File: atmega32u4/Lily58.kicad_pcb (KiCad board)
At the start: 2 copper layers, 142.5 x 106.3 mm, 96 parts, among them J2 4PIN, J4 USB_C_Receptacle_USB2.0, P4 OLED, SW1 SW_PUSH, SW10 SW_PUSH, SW11 SW_PUSH, SW12 SW_PUSH, SW13 SW_PUSH, SW14 SW_PUSH, SW15 SW_PUSH, SW16 SW_PUSH, SW17 SW_PUSH, SW18 SW_PUSH, SW19 SW_PUSH, SW2 SW_PUSH, SW20 SW_PUSH, SW21 SW_PUSH, SW22 SW_PUSH, SW23 SW_PUSH, SW24 SW_PUSH, SW25 SW_PUSH, SW26 SW_PUSH, SW27 SW_PUSH, SW28 SW_PUSH, SW29 SW_PUSH, SW3 SW_PUSH, SW4 SW_PUSH, SW5 SW_PUSH, SW6 SW_PUSH, SW7 SW_PUSH, SW8 SW_PUSH, SW9 SW_PUSH, U1 ATmega32U4-AU, U2 MCP23017_SO, U3 MCP1703A-3302_SOT23, Y1 16MHz

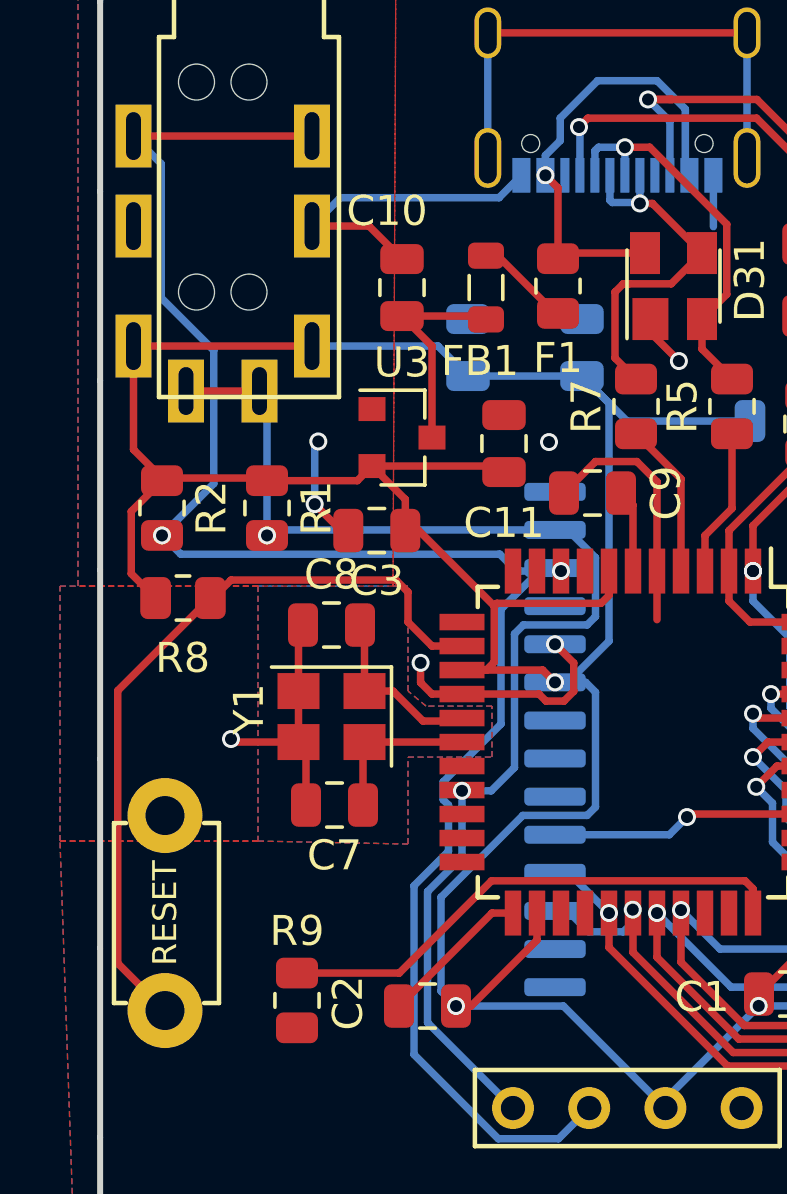
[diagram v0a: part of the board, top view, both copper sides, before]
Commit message: removing ldo on atmega32u4
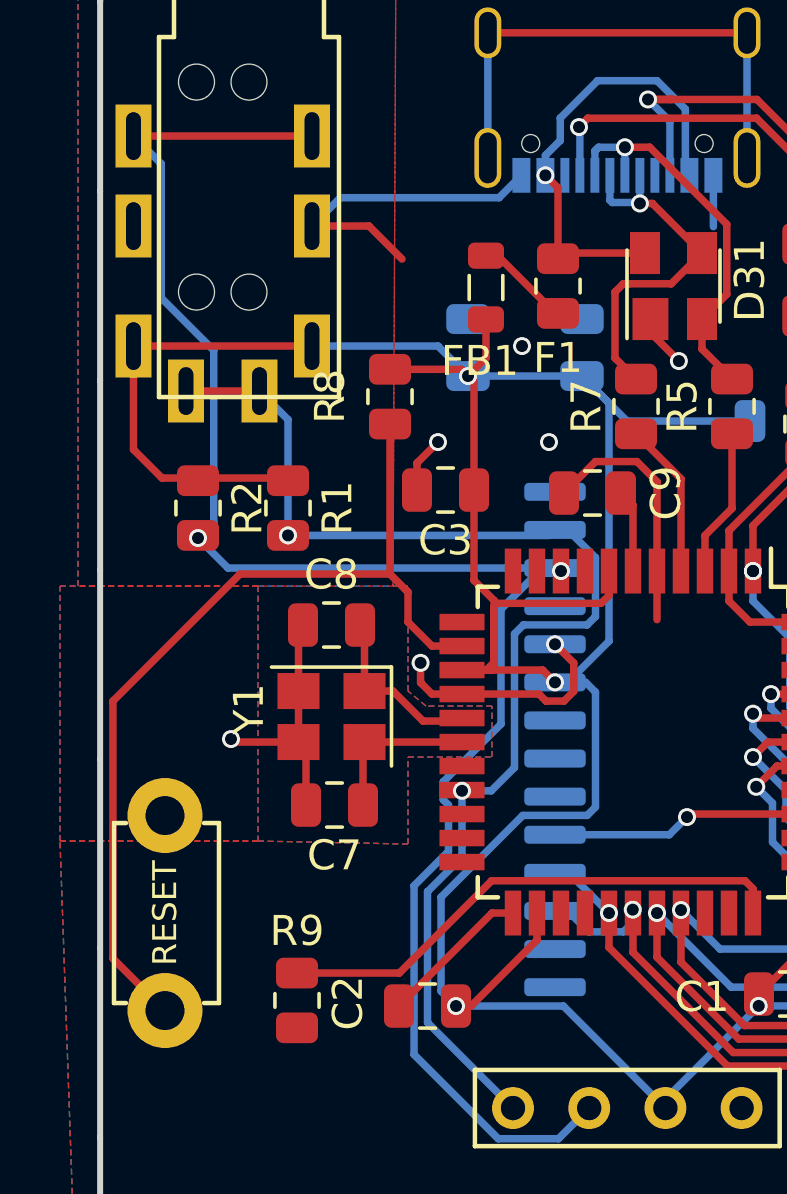
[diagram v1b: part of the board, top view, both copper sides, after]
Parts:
- removed C10, C11: 1uF, Capacitor_SMD:C_0805_2012Metric
- removed U3: MCP1703A-3302_SOT23, Package_TO_SOT_SMD:SOT-23
- moved R8 9.63 mm to (92.6, 51.3), turned to 270 degrees
- moved C3 2.66 mm to (94.5, 54.4)
- moved R2 1.20 mm to (86.2, 55.0)
- moved R1 0.70 mm to (89.2, 55.0)
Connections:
- C1 pad 1: +3V3 -> +5V
- C2 pad 1: +3V3 -> +5V
- C3 pad 1: +3V3 -> +5V
- C4 pad 1: +3V3 -> +5V
- C5 pad 1: +3V3 -> +5V
- C6 pad 1: +3V3 -> +5V
- J2 pad 1: +3V3 -> +5V
- P4 pad 3: +3V3 -> +5V
- R1 pad 1: +3V3 -> +5V
- R2 pad 1: +3V3 -> +5V
- R3 pad 2: +3V3 -> +5V
- R8 pad 1: +3V3 -> +5V
- U1 pad 14: +3V3 -> +5V
- U1 pad 2: +3V3 -> +5V
- U1 pad 24: +3V3 -> +5V
- U1 pad 34: +3V3 -> +5V
- U1 pad 44: +3V3 -> +5V
- U1 pad 7: +3V3 -> +5V
- U2 pad 3: row3 -> row4
- U2 pad 4: row4 -> row3
- U2 pad 9: +3V3 -> +5V
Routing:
- net +3V3: track 144.6 -> 0.00 mm, vias 4 -> 0
- net +5V: track 7.31 -> 141.5 mm, vias 0 -> 5
- net Net-(R8-Pad2): track 26.0 -> 31.1 mm
- net GND: track 58.7 -> 56.6 mm
- net SCL: track 62.6 -> 60.8 mm
